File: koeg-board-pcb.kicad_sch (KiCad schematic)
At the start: 73 parts, among them J1 Conn_01x02, J2 USB_C_Receptacle_USB2.0_14P, J3 SWD_Connector, SW1 SW_Push, SW10 SW_Push, SW11 SW_Push, SW12 SW_Push, SW13 SW_Push, SW14 SW_Push, SW15 SW_Push, SW16 SW_Push, SW17 SW_Push, SW18 SW_Push, SW19 SW_Push, SW2 Reset Button, SW20 SW_Push, SW21 SW_Push, SW22 SW_Push, SW23 SW_Push, SW3 SW_DPST, SW4 SW_Push, SW5 SW_Push, SW6 SW_Push, SW7 SW_Push, SW8 SW_Push, SW9 SW_Push, U1 nRF52840, Y1 32MHz

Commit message: before auto route
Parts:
- removed SW3: SW_DPST, symbol Switch:SW_DPST
- removed Y1: 32MHz, symbol Device:Crystal
- added C16: 100nF, Capacitor_SMD:C_0402_1005Metric, symbol Device:C
- added F1: 500mA, Fuse:Fuse_0603_1608Metric, symbol Device:Fuse
- added H1, H2, H3, H4, H5: MountingHole, MountingHole:MountingHole_2mm, symbol Mechanical:MountingHole
- added R7: 100K, Resistor_SMD:R_0201_0603Metric, symbol Device:R
- added SW3: SW_On_Off, Button_Switch_THT:SW_CK_JS202011AQN_DPDT_Angled, symbol Switch:SW_DPDT_x2
- added U3: USBLC6-2SC6, Package_TO_SOT_SMD:SOT-23-6, symbol Power_Protection:USBLC6-2SC6
- added Y1: Crystal_GND2, Crystal:Crystal_SMD_2016-4Pin_2.0x1.6mm, symbol Device:Crystal_GND2
- C1, C10, C11, C2, C3, C4, C6, C7: footprint (none) -> Capacitor_SMD:C_0402_1005Metric
- C12, C13, C8, C9: value 4.7μF -> 4.7uF; footprint (none) -> Capacitor_SMD:C_0402_1005Metric
- C5: value 1μF -> 1uF; footprint (none) -> Capacitor_SMD:C_0402_1005Metric
- D1, D10, D11, D12, D13, D14, D15, D16, D17, D18, D19, D20, D21, D22, D3, D4, D5, D6, D7, D8, D9: footprint (none) -> Diode_SMD:D_SOD-123
- D2: value D -> 1N5819; footprint (none) -> Diode_SMD:D_SOD-123
- J1: footprint (none) -> Connector_PinHeader_1.00mm:PinHeader_1x02_P1.00mm_Vertical
- J2: footprint (none) -> Connector_USB:USB_C_Receptacle_G-Switch_GT-USB-7010ASV
- J3: footprint (none) -> Connector_PinHeader_1.00mm:PinHeader_1x04_P1.00mm_Vertical
- L1, L3: value 10μH -> 10uH; footprint (none) -> Inductor_SMD:L_0201_0603Metric
- L2, L4, L5: footprint (none) -> Inductor_SMD:L_0201_0603Metric
- R1, R2, R3, R4: footprint (none) -> Resistor_SMD:R_0201_0603Metric
- SW1, SW10, SW11, SW12, SW13, SW14, SW15, SW16, SW17, SW18, SW19, SW20, SW21, SW22, SW4, SW5, SW6, SW7, SW8, SW9: footprint (none) -> PCM_Switch_Keyboard_Hotswap_Kailh:SW_Hotswap_Kailh_Choc_V1V2_1.00u
- SW2: footprint (none) -> Button_Switch_SMD:SW_SPST_TL3342
- SW23: footprint (none) -> PCM_Switch_Keyboard_Hotswap_Kailh:SW_Hotswap_Kailh_Choc_V1V2_1.75u_90deg
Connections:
- net nRF_VDD is gone; now on net V_SYS: J3.2 (Pin_2), U1.A22 (VDD), U1.AD14 (VDD), U1.AD23 (VDD), U1.B1 (VDD), U1.W1 (VDD)
- net COL0: now also U1.R24 (P1.06); no longer U1.AD8 (P0.13)
- net COL1: now also U1.AD20 (P0.24); no longer U1.AC9 (P0.14)
- net COL2: now also U1.U24 (P1.04); no longer U1.AD10 (P0.15)
- net COL3: now also U1.W24 (P1.02); no longer U1.AC11 (P0.16)
- net COL4: now also U1.N1 (P0.08); no longer U1.AD12 (P0.17)
- net D+: now also U3.3 (I/O2), U3.4 (I/O2)
- net D-: now also U3.1 (I/O1), U3.6 (I/O1)
- net GND: now also C13.2, C16.1, U3.2 (GND), Y1.2; no longer C13.1
- net LED_PIN: now also U1.A12 (AIN0/P0.02); no longer U1.AD20 (P0.24)
- net RESET: now also C16.2, R7.2
- net ROW0: now also U1.A8 (AIN7/P0.31); no longer U1.AC15 (P0.19)
- net ROW1: now also U1.R1 (TRACEDATA3/P1.09); no longer U1.AD16 (P0.20)
- net ROW2: now also U1.A16 (P1.13); no longer U1.AC17 (P0.21)
- net ROW3: now also U1.A14 (P1.15); no longer U1.AD18 (P0.22)
- net ROW4: now also U1.A10 (AIN5/P0.29); no longer U1.AC19 (P0.23)
- net VBAT: now also SW3.2 (B)
- net VBUS: now also F1.2; no longer D2.2 (A)
- net XC1: now also Y1.3
- net XC2: now also Y1.1
- net VDD renamed V_SYS
- net V_SYS: now also R7.1
- net nRF_VBUS renamed 5V
- net 5V: now also C12.1, D2.2 (A), F1.1, U3.5 (VBUS); no longer C13.2
- net nRF_VDDH renamed 3.2V-5V
- net 3.2V-5V: now also C13.1, SW3.3 (C); no longer C12.1
- no-connect marks 36 -> 37
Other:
- removed sheet LEDs
- added sheet leds (leds.kicad_sch)
- note added: "ESD"
- note added: "flag"

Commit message: one side done
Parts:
- removed Y1: Crystal_GND2, Crystal:Crystal_SMD_2016-4Pin_2.0x1.6mm, symbol Device:Crystal_GND2
- added Y2: JYJE 2TJ432000NYFBC, Crystal:Crystal_SMD_2520-4Pin_2.5x2.0mm, symbol Device:Crystal_GND24
- J2: footprint Connector_USB:USB_C_Receptacle_G-Switch_GT-USB-7010ASV -> USB_Type_C:HRO-TYPE-C-31-M-12; LCSC (none) -> C165948
- L1, L3: footprint Inductor_SMD:L_0201_0603Metric -> Inductor_SMD:L_1008_2520Metric; LCSC (none) -> C280469
- R3: value 2M -> 10K
- R4: value 810K -> 10K
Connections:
- net DECUSB: now also U1.AD8 (P0.13)
- net GND: now also Y2.2, Y2.4
- net RESET: now also U1.AD12 (P0.17)
- net XC1: now also Y2.1
- net XC2: now also Y2.3
- no-connect marks 37 -> 35

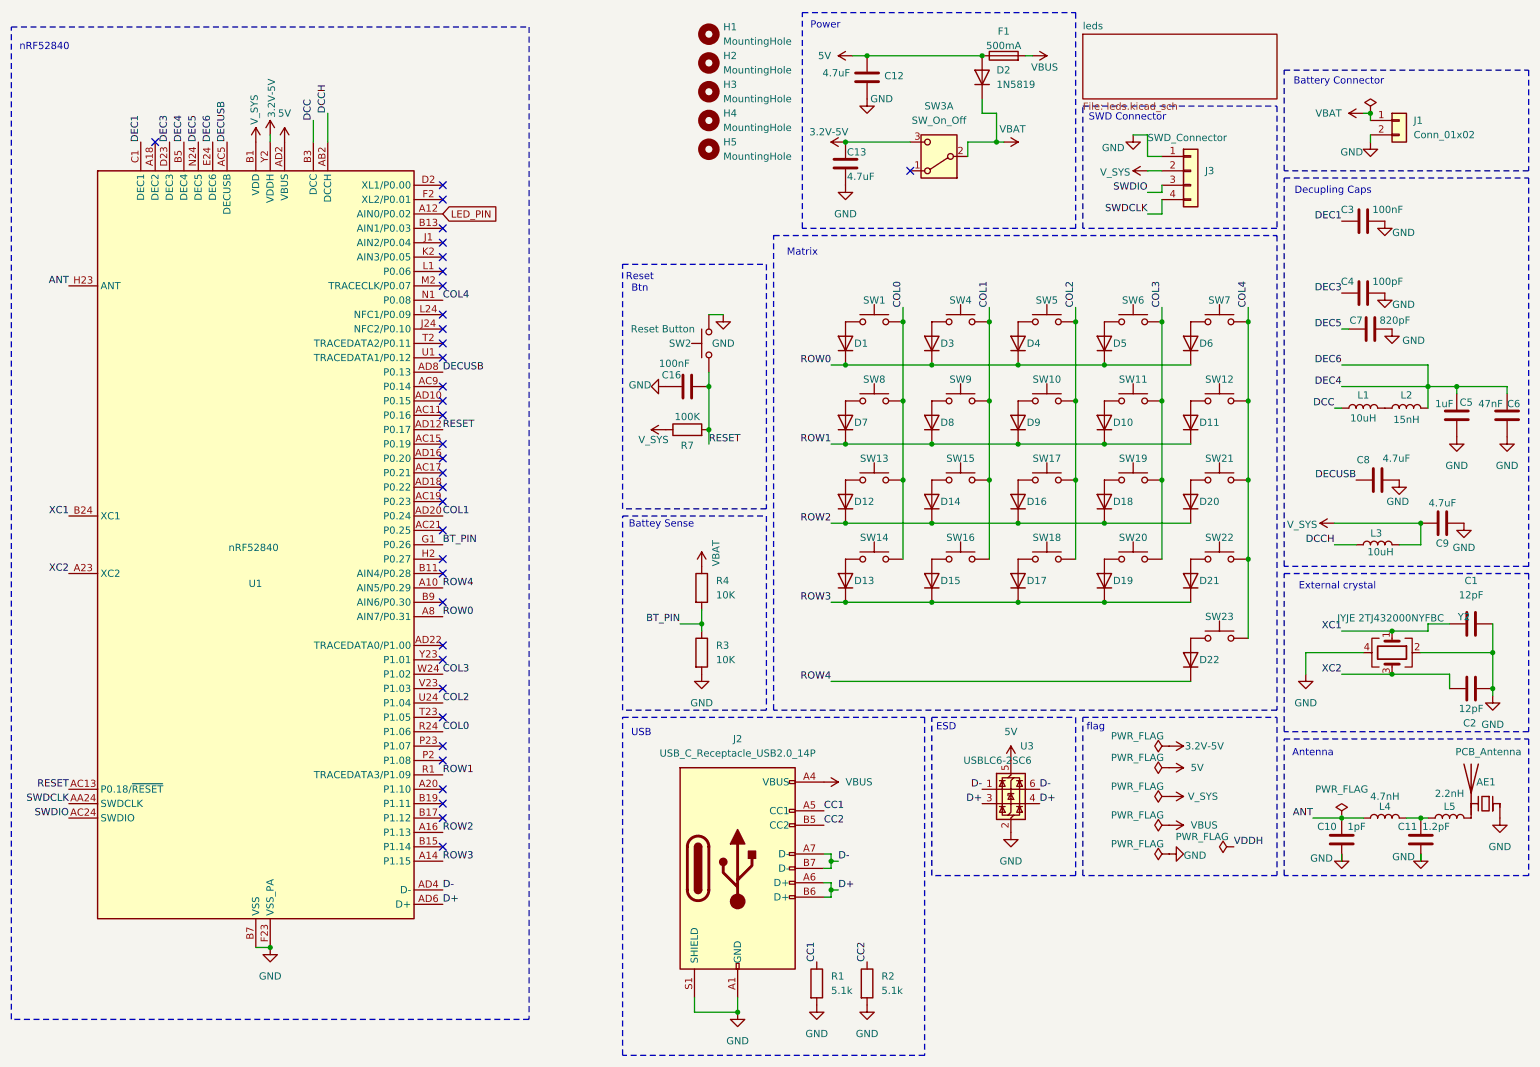
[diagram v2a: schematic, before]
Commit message: reassigned basic components, now comes the leds
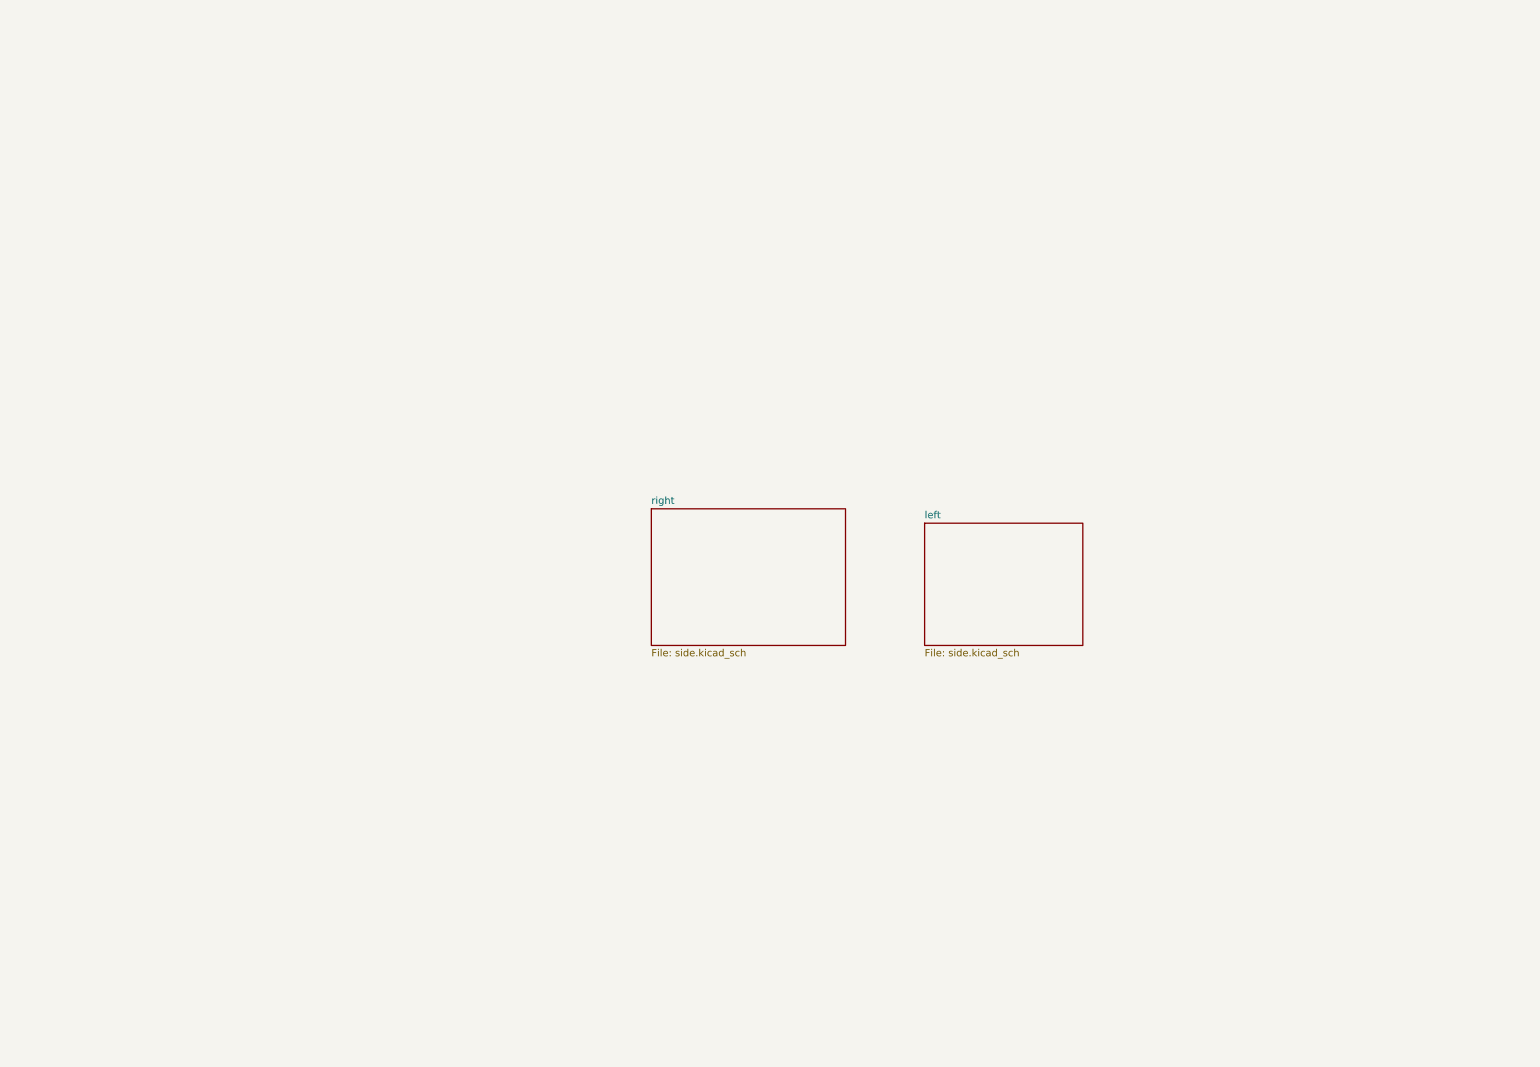
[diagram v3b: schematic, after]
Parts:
- removed AE1: PCB_Antenna, pcb_ant:pcb_antenna, symbol Device:Antenna_Chip
- removed C1, C2: 12pF, Capacitor_SMD:C_0402_1005Metric, symbol Device:C
- removed C10: 1pF, Capacitor_SMD:C_0402_1005Metric, symbol Device:C
- removed C11: 1.2pF, Capacitor_SMD:C_0402_1005Metric, symbol Device:C
- removed C12, C13, C8, C9: 4.7uF, Capacitor_SMD:C_0402_1005Metric, symbol Device:C
- removed C16, C3: 100nF, Capacitor_SMD:C_0402_1005Metric, symbol Device:C
- removed C4: 100pF, Capacitor_SMD:C_0402_1005Metric, symbol Device:C
- removed C5: 1uF, Capacitor_SMD:C_0402_1005Metric, symbol Device:C
- removed C6: 47nF, Capacitor_SMD:C_0402_1005Metric, symbol Device:C
- removed C7: 820pF, Capacitor_SMD:C_0402_1005Metric, symbol Device:C
- removed D1, D10, D11, D12, D13, D14, D15, D16, D17, D18, D19, D2, D20, D21, D22, D3, D4, D5, D6, D7, D8, D9: 1N5819, Diode_SMD:D_SOD-123, symbol Device:D
- removed F1: 500mA, Fuse:Fuse_0603_1608Metric, symbol Device:Fuse
- removed H1, H2, H3, H4, H5: MountingHole, MountingHole:MountingHole_2mm, symbol Mechanical:MountingHole
- removed J1: Conn_01x02, Connector_PinHeader_1.00mm:PinHeader_1x02_P1.00mm_Vertical, symbol Connector_Generic:Conn_01x02
- removed J2: USB_C_Receptacle_USB2.0_14P, USB_Type_C:HRO-TYPE-C-31-M-12, symbol Connector:USB_C_Receptacle_USB2.0_14P
- removed J3: SWD_Connector, Connector_PinHeader_1.00mm:PinHeader_1x04_P1.00mm_Vertical, symbol Connector_Generic:Conn_01x04
- removed L1, L3: 10uH, Inductor_SMD:L_1008_2520Metric, symbol Device:L
- removed L2: 15nH, Inductor_SMD:L_0201_0603Metric, symbol Device:L
- removed L4: 4.7nH, Inductor_SMD:L_0201_0603Metric, symbol Device:L
- removed L5: 2.2nH, Inductor_SMD:L_0201_0603Metric, symbol Device:L
- removed R1, R2: 5.1k, Resistor_SMD:R_0201_0603Metric, symbol Device:R
- removed R3, R4: 10K, Resistor_SMD:R_0201_0603Metric, symbol Device:R
- removed R7: 100K, Resistor_SMD:R_0201_0603Metric, symbol Device:R
- removed SW1, SW10, SW11, SW12, SW13, SW14, SW15, SW16, SW17, SW18, SW19, SW20, SW21, SW22, SW4, SW5, SW6, SW7, SW8, SW9: SW_Push, PCM_Switch_Keyboard_Hotswap_Kailh:SW_Hotswap_Kailh_Choc_V1V2_1.00u, symbol Switch:SW_Push
- removed SW2: Reset Button, Button_Switch_SMD:SW_SPST_TL3342, symbol Switch:SW_Push
- removed SW23: SW_Push, PCM_Switch_Keyboard_Hotswap_Kailh:SW_Hotswap_Kailh_Choc_V1V2_1.75u_90deg, symbol Switch:SW_Push
- removed SW3: SW_On_Off, Button_Switch_THT:SW_CK_JS202011AQN_DPDT_Angled, symbol Switch:SW_DPDT_x2
- removed U1: nRF52840, Package_DFN_QFN:Nordic_AQFN-73-1EP_7x7mm_P0.5mm, symbol MCU_Nordic:nRF52840
- removed U3: USBLC6-2SC6, Package_TO_SOT_SMD:SOT-23-6, symbol Power_Protection:USBLC6-2SC6
- removed Y2: JYJE 2TJ432000NYFBC, Crystal:Crystal_SMD_2520-4Pin_2.5x2.0mm, symbol Device:Crystal_GND24
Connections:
- no-connect marks 35 -> 0
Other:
- removed sheet leds
- added sheet left (side.kicad_sch)
- added sheet right (side.kicad_sch)
- note removed: "Antenna"
- note removed: "Battery Connector"
- note removed: "Battey Sense"
- note removed: "Decupling Caps"
- note removed: "ESD"
- note removed: "External crystal"
- note removed: "Matrix"
- note removed: "Power"
- note removed: "Reset Btn"
- note removed: "SWD Connector"
- note removed: "USB"
- note removed: "flag"
- note removed: "nRF52840"

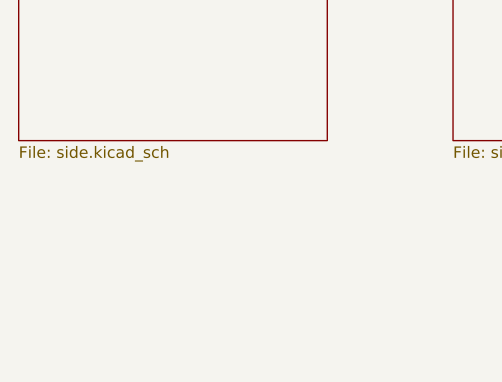
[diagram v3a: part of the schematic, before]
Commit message: the right side still needs to be routed
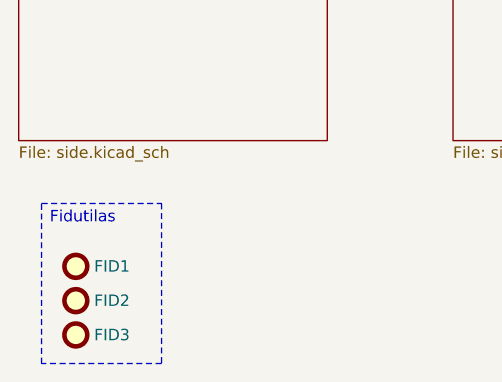
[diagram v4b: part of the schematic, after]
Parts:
- added FID1, FID2, FID3: Fiducial, Fiducial:Fiducial_1.5mm_Mask3mm, symbol Mechanical:Fiducial
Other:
- note added: "Fidutilas"
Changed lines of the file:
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@@
 	(generator_version "8.0")
 	(paper "A4")
+	(rectangle
+		(start 130.81 131.445)
+		(end 144.145 149.225)
+		(stroke
+			(width 0)
+			(type dash)
+		)
+		(fill
+			(type none)
+		)
+	)
+	(text "Fidutilas\n\n"
+		(exclude_from_sim no)
+		(at 135.382 134.112 0)
+		(effects
+			(font
+				(size 1.27 1.27)
+			)
+		)
+	)
+	(symbol
+		(lib_id "Mechanical:Fiducial")
+		(at 134.62 142.24 0)
+		(unit 1)
+		(exclude_from_sim yes)
+		(in_bom no)
+		(on_board yes)
+		(dnp no)
+		(property "Reference" "FID2"
+			(at 136.652 142.24 0)
+			(effects
+				(font
+					(size 1.27 1.27)
+				)
+				(justify left)
+			)
+		)
+		(property "Value" "Fiducial"
+			(at 137.16 143.5099 0)
+			(effects
+				(font
+					(size 1.27 1.27)
+				)
+				(justify left)
+				(hide yes)
+			)
+		)
+		(property "Footprint" "Fiducial:Fiducial_1.5mm_Mask3mm"
+			(at 134.62 142.24 0)
+			(effects
+				(font
+					(size 1.27 1.27)
+				)
+				(hide yes)
+			)
+		)
+		(property "Datasheet" "~"
+			(at 134.62 142.24 0)
+			(effects
+				(font
+					(size 1.27 1.27)
+				)
+				(hide yes)
+			)
+		)
+		(property "Description" "Fiducial Marker"
+			(at 134.62 142.24 0)
+			(effects
+				(font
+					(size 1.27 1.27)
+				)
+				(hide yes)
+			)
+		)
+		(instances
+			(project "koeg-board-pcb"
+				(path "/2b736a6b-c6e2-42fa-94c9-e384d663659b"
+					(reference "FID2")
+					(unit 1)
+				)
+			)
+		)
+	)
+	(symbol
+		(lib_id "Mechanical:Fiducial")
+		(at 134.62 138.43 0)
+		(unit 1)
+		(exclude_from_sim yes)
+		(in_bom no)
+		(on_board yes)
+		(dnp no)
+		(property "Reference" "FID1"
+			(at 136.652 138.43 0)
+			(effects
+				(font
+					(size 1.27 1.27)
+				)
+				(justify left)
+			)
+		)
+		(property "Value" "Fiducial"
+			(at 137.16 139.6999 0)
+			(effects
+				(font
+					(size 1.27 1.27)
+				)
+				(justify left)
+				(hide yes)
+			)
+		)
+		(property "Footprint" "Fiducial:Fiducial_1.5mm_Mask3mm"
+			(at 134.62 138.43 0)
+			(effects
+				(font
+					(size 1.27 1.27)
+				)
+				(hide yes)
+			)
+		)
+		(property "Datasheet" "~"
+			(at 134.62 138.43 0)
+			(effects
+				(font
+					(size 1.27 1.27)
+				)
+				(hide yes)
+			)
+		)
+		(property "Description" "Fiducial Marker"
+			(at 134.62 138.43 0)
+			(effects
+				(font
+					(size 1.27 1.27)
+				)
+				(hide yes)
+			)
+		)
+		(instances
+			(project "koeg-board-pcb"
+				(path "/2b736a6b-c6e2-42fa-94c9-e384d663659b"
+					(reference "FID1")
+					(unit 1)
+				)
+			)
+		)
+	)
+	(symbol
+		(lib_id "Mechanical:Fiducial")
+		(at 134.62 146.05 0)
+		(unit 1)
+		(exclude_from_sim yes)
+		(in_bom no)
+		(on_board yes)
+		(dnp no)
+		(property "Reference" "FID3"
+			(at 136.652 146.05 0)
+			(effects
+				(font
+					(size 1.27 1.27)
+				)
+				(justify left)
+			)
+		)
+		(property "Value" "Fiducial"
+			(at 137.16 147.3199 0)
+			(effects
+				(font
+					(size 1.27 1.27)
+				)
+				(justify left)
+				(hide yes)
+			)
+		)
+		(property "Footprint" "Fiducial:Fiducial_1.5mm_Mask3mm"
+			(at 134.62 146.05 0)
+			(effects
+				(font
+					(size 1.27 1.27)
+				)
+				(hide yes)
+			)
+		)
+		(property "Datasheet" "~"
+			(at 134.62 146.05 0)
+			(effects
+				(font
+					(size 1.27 1.27)
+				)
+				(hide yes)
+			)
+		)
+		(property "Description" "Fiducial Marker"
+			(at 134.62 146.05 0)
+			(effects
+				(font
+					(size 1.27 1.27)
+				)
+				(hide yes)
+			)
+		)
+		(instances
+			(project "koeg-board-pcb"
+				(path "/2b736a6b-c6e2-42fa-94c9-e384d663659b"
+					(reference "FID3")
+					(unit 1)
+				)
+			)
+		)
+	)
 	(sheet
 		(at 176.53 102.87)

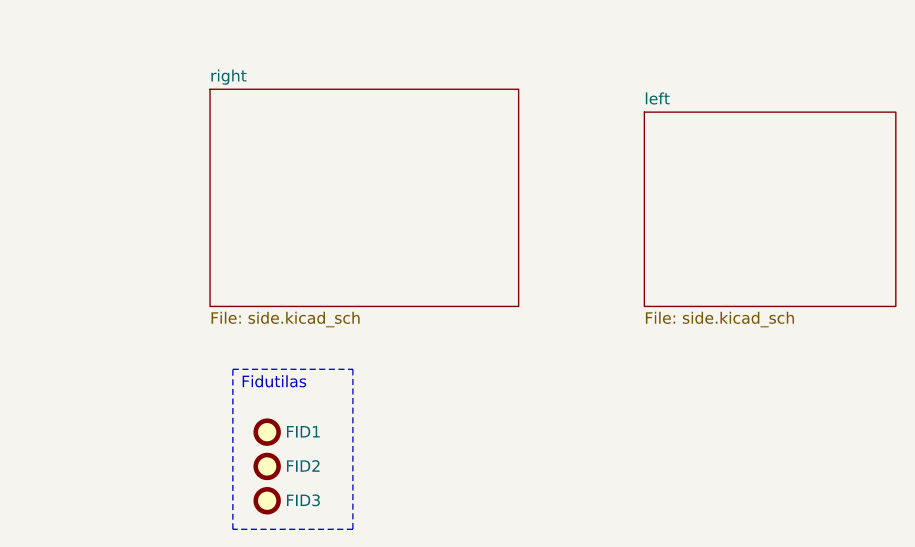
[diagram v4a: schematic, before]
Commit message: finished power circuit
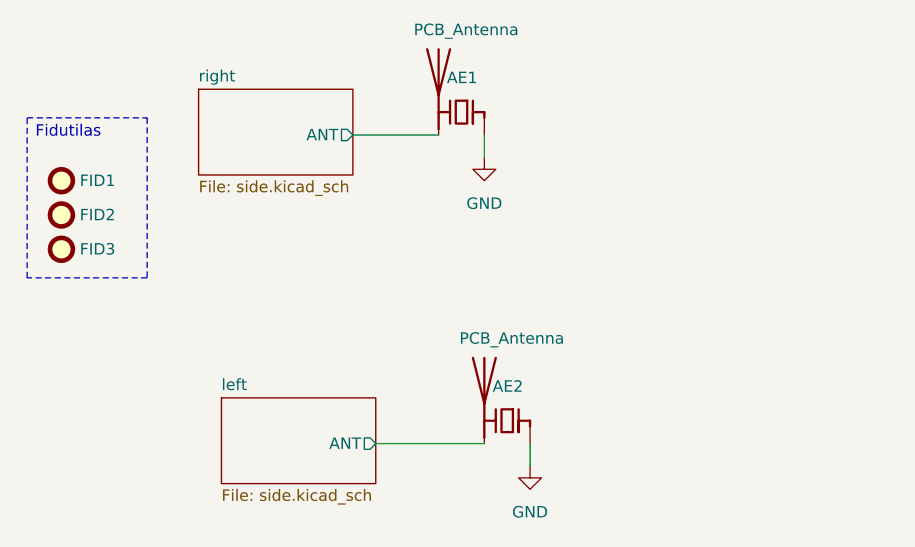
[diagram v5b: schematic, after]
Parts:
- added AE1: PCB_Antenna, pcb_ant:flipped_pcb_antenna, symbol Device:Antenna_Chip
- added AE2: PCB_Antenna, pcb_ant:pcb_antenna, symbol Device:Antenna_Chip
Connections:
- new net GND: AE1.1 (FEED), AE2.1 (FEED)
- new net left/ANT: AE2.2 (PCB_Trace)
- new net right/ANT: AE1.2 (PCB_Trace)
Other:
- sheet left ports: added ANT; removed none
- sheet right ports: added ANT; removed none
- moved on the sheet: FID1, FID2, FID3
